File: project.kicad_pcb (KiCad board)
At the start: 4 copper layers, 114.3 x 48.3 mm, 30 parts, among them J1 Conn_01x02, J2 Conn_01x15, J3 Conn_01x15, J4 Conn_01x02, J5 Conn_01x02, J6 Conn_01x02, U1 DRV8870DDA, U2 DRV8870DDA, U3 DRV8870DDA

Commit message: Add labels to terminal blocks
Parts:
- added REF**: OSHW-Logo2_9.8x8mm_SilkScreen, Symbol:OSHW-Logo2_9.8x8mm_SilkScreen, F.Cu at (80.9, 110.1)
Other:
- board text added: "36V"
- board text added: "UBC Orbit Helmholtz Driver Rev 1"
- board text added: "X"
- board text added: "Y"
- board text added: "Z"

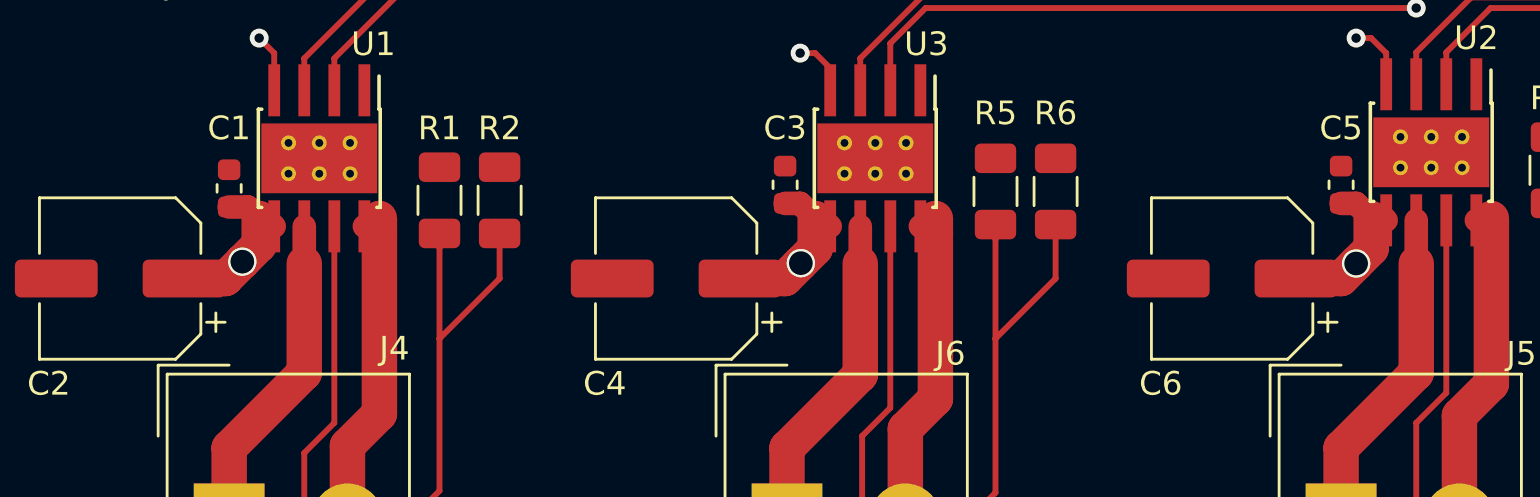
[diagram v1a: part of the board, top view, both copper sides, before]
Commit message: Replace 36V input to drivers with solid fill
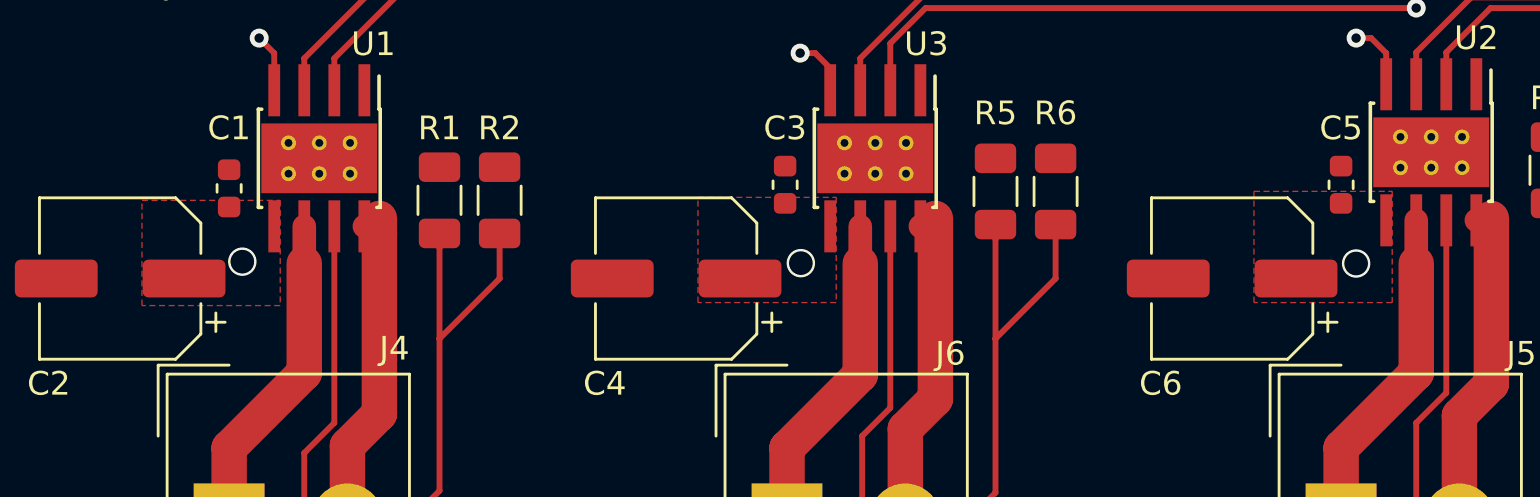
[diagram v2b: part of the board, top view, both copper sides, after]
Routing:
- net +36V: track 21.6 -> 0.00 mm
- added copper zone on F.Cu, net +36V
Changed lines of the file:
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@@
     (thickness 1.6)
     (drawings 26)
-    (tracks 197)
+    (tracks 173)
     (zones 0)
     (modules 31)
@@
   (segment (start 118.11 140.97) (end 120.65 140.97) (width 0.25) (layer F.Cu) (net 6))
   (segment (start 116.84 139.7) (end 118.11 140.97) (width 0.25) (layer F.Cu) (net 6))
-  (segment (start 124.46 115.57) (end 120.65 115.57) (width 0.25) (layer F.Cu) (net 40))
-  (segment (start 139.7 115.57) (end 143.51 115.57) (width 0.25) (layer F.Cu) (net 39))
   (segment (start 120.65 138.43) (end 124.46 138.43) (width 0.25) (layer F.Cu) (net 7))
   (segment (start 112.767802 121.019982) (end 117.475 125.72718) (width 0.25) (layer F.Cu) (net 7))
@@
   (segment (start 139.7 143.51) (end 143.51 143.51) (width 0.25) (layer F.Cu) (net 26))
   (segment (start 124.46 110.49) (end 120.65 110.49) (width 0.25) (layer F.Cu) (net 27))
-  (segment (start 98.425 133.35) (end 100.33 133.35) (width 1.5) (layer F.Cu) (net 28))
-  (segment (start 100.33 133.35) (end 100.965 132.715) (width 1.5) (layer F.Cu) (net 28))
-  (segment (start 101.6 132.08) (end 101.6 130.81) (width 1.5) (layer F.Cu) (net 28))
-  (segment (start 74.93 133.35) (end 76.835 133.35) (width 1.5) (layer F.Cu) (net 28))
-  (segment (start 76.835 133.35) (end 77.47 132.715) (width 1.5) (layer F.Cu) (net 28))
-  (segment (start 78.105 132.08) (end 78.105 130.81) (width 1.5) (layer F.Cu) (net 28))
-  (segment (start 53.185 133.35) (end 53.8975 132.6375) (width 1.5) (layer F.Cu) (net 28))
-  (segment (start 51.435 133.35) (end 53.185 133.35) (width 1.5) (layer F.Cu) (net 28))
-  (segment (start 54.61 131.925) (end 54.61 130.81) (width 1.5) (layer F.Cu) (net 28))
   (segment (start 77.47 132.715) (end 77.47 132.715) (width 1.5) (layer F.Cu) (net 28))
   (via (at 77.5 132.7) (size 1.2) (drill 1) (layers F.Cu B.Cu) (net 28))
-  (segment (start 77.47 132.715) (end 78.105 132.08) (width 1.5) (layer F.Cu) (net 28))
-  (segment (start 100.965 132.715) (end 101.6 132.08) (width 1.5) (layer F.Cu) (net 28))
   (via (at 100.965 132.715) (size 1.2) (drill 1) (layers F.Cu B.Cu) (net 28))
-  (segment (start 53.8975 132.6375) (end 54.61 131.925) (width 1.5) (layer F.Cu) (net 28))
   (via (at 53.8975 132.6375) (size 1.2) (drill 1) (layers F.Cu B.Cu) (net 28))
-  (segment (start 77.47 130.175) (end 78.105 130.81) (width 1) (layer F.Cu) (net 28))
-  (segment (start 76.835 130.175) (end 77.47 130.175) (width 1) (layer F.Cu) (net 28))
-  (segment (start 78.405 130.81) (end 78.74 131.145) (width 1) (layer F.Cu) (net 28))
-  (segment (start 78.105 130.81) (end 78.405 130.81) (width 1) (layer F.Cu) (net 28))
-  (segment (start 100.965 130.175) (end 101.6 130.81) (width 1) (layer F.Cu) (net 28))
-  (segment (start 100.33 130.175) (end 100.965 130.175) (width 1) (layer F.Cu) (net 28))
-  (segment (start 102.154 130.81) (end 102.235 130.891) (width 1) (layer F.Cu) (net 28))
-  (segment (start 101.6 130.81) (end 102.154 130.81) (width 1) (layer F.Cu) (net 28))
-  (segment (start 54.1275 130.3275) (end 54.61 130.81) (width 1) (layer F.Cu) (net 28))
-  (segment (start 53.34 130.3275) (end 54.1275 130.3275) (width 1) (layer F.Cu) (net 28))
-  (segment (start 54.91 130.81) (end 55.245 131.145) (width 1) (layer F.Cu) (net 28))
-  (segment (start 54.61 130.81) (end 54.91 130.81) (width 1) (layer F.Cu) (net 28))
   (segment (start 58.34 143.51) (end 58.34 140.415) (width 1.5) (layer F.Cu) (net 29))
   (segment (start 58.34 140.415) (end 59.69 139.065) (width 1.5) (layer F.Cu) (net 29))
@@
   (segment (start 63.627 116.205) (end 63.5 116.332) (width 0.25) (layer F.Cu) (net 38))
   (segment (start 69.85 116.205) (end 63.627 116.205) (width 0.25) (layer F.Cu) (net 38))
+  (segment (start 139.7 115.57) (end 143.51 115.57) (width 0.25) (layer F.Cu) (net 39))
+  (segment (start 124.46 115.57) (end 120.65 115.57) (width 0.25) (layer F.Cu) (net 40))
   (zone (net 5) (net_name GND) (layer F.Cu) (hatch edge 0.508)
     (connect_pads (clearance 0.508))
@@
       )
     )
+  )
+  (zone (net 28) (net_name +36V) (layer F.Cu) (hatch edge 0.508)
+    (priority 1)
+    (connect_pads yes (clearance 0.508))
+    (min_thickness 0.254)
+    (fill yes (arc_segments 32) (thermal_gap 0.508) (thermal_bridge_width 0.508))
+    (polygon
+      (pts
+        (xy 55.499 134.493) (xy 49.657 134.493) (xy 49.657 130.048) (xy 55.499 130.048)
+      )
+    )
+  )
+  (zone (net 28) (net_name +36V) (layer F.Cu) (hatch edge 0.508)
+    (priority 1)
+    (connect_pads yes (clearance 0.508))
+    (min_thickness 0.254)
+    (fill yes (arc_segments 32) (thermal_gap 0.508) (thermal_bridge_width 0.508))
+    (polygon
+      (pts
+        (xy 78.994 134.366) (xy 73.152 134.366) (xy 73.152 129.921) (xy 78.994 129.921)
+      )
+    )
+  )
+  (zone (net 28) (net_name +36V) (layer F.Cu) (hatch edge 0.508)
+    (priority 1)
+    (connect_pads yes (clearance 0.508))
+    (min_thickness 0.254)
+    (fill yes (arc_segments 32) (thermal_gap 0.508) (thermal_bridge_width 0.508))
+    (polygon
+      (pts
+        (xy 102.489 134.366) (xy 96.647 134.366) (xy 96.647 129.667) (xy 102.489 129.667)
+      )
+    )

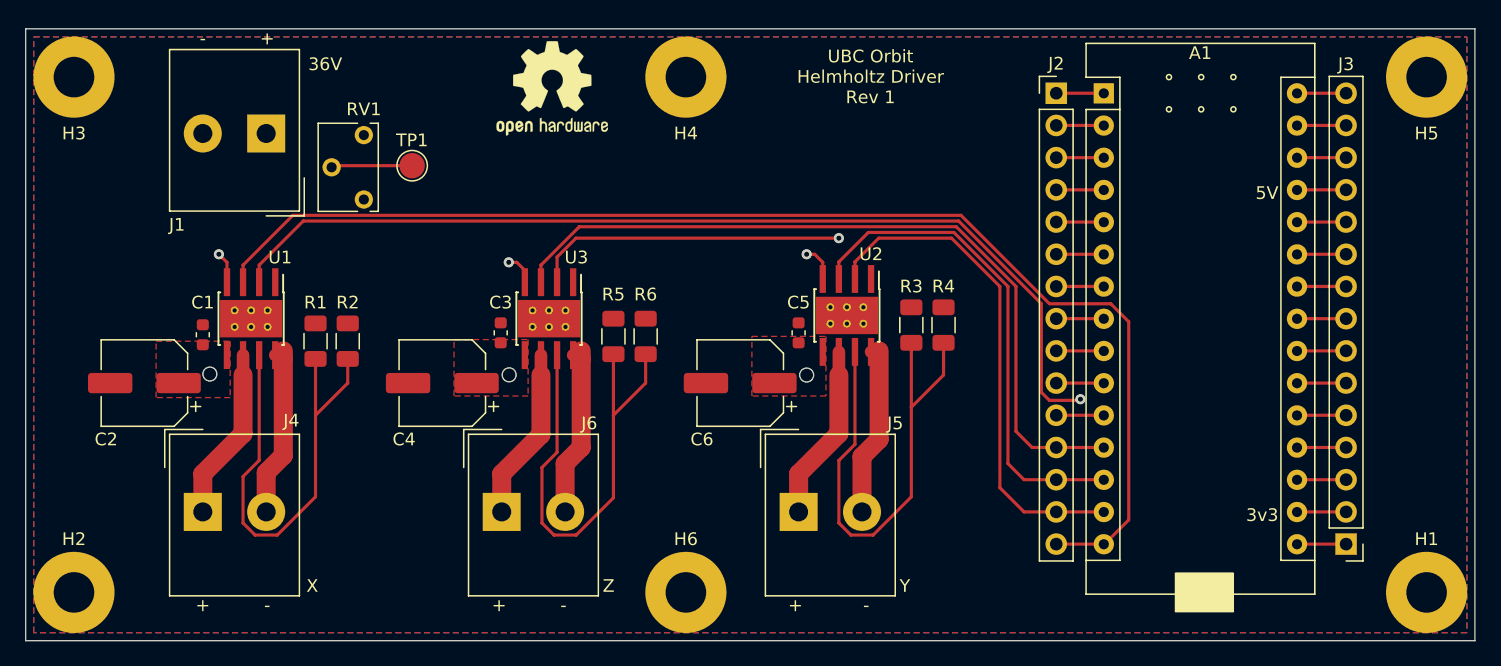
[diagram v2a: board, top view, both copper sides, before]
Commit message: Convert board to 2 layer
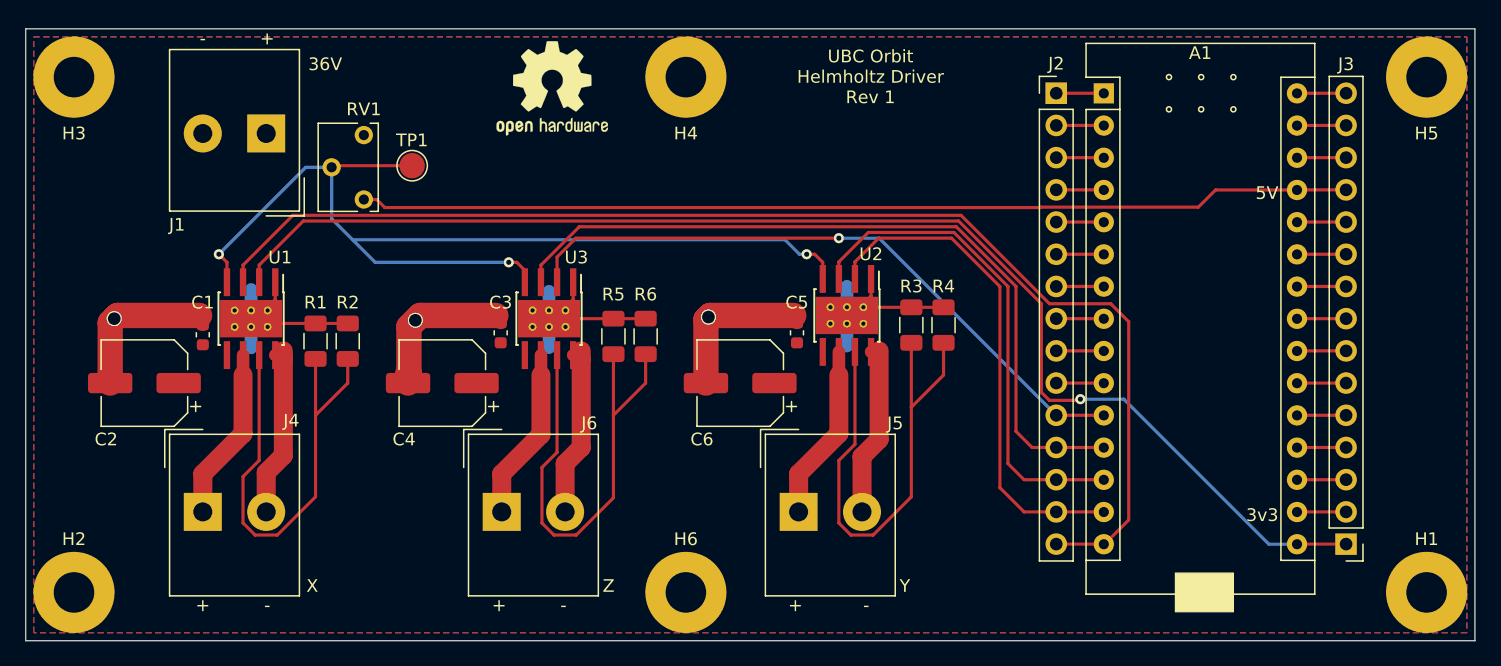
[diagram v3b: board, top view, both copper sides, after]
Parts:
- moved C5 0.13 mm to (100.2, 129.4)
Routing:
- net GND: track 7.62 -> 94.6 mm, vias 0 -> 3
- net IN_Z_2: track 56.0 -> 51.6 mm
- net +36V: vias 3 -> 0
- removed copper zone on In1.Cu, net +36V
- removed copper zone on F.Cu, net GND
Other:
- copper layers 4 -> 2
